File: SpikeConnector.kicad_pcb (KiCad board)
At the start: 2 copper layers, 12 x 40 mm, 4 parts

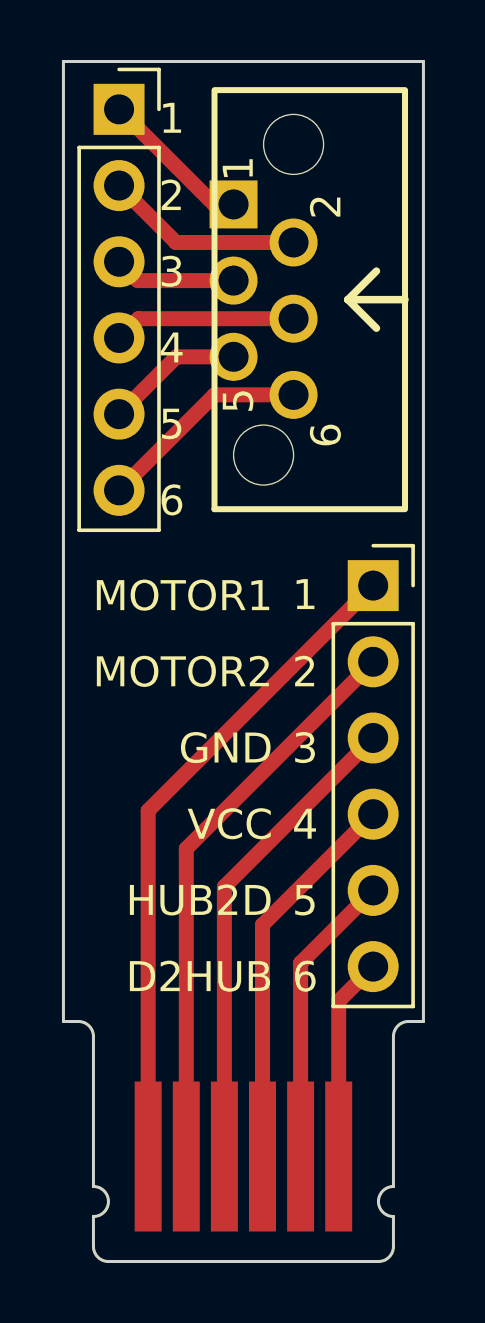
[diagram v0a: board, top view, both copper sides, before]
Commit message: Male connector fix
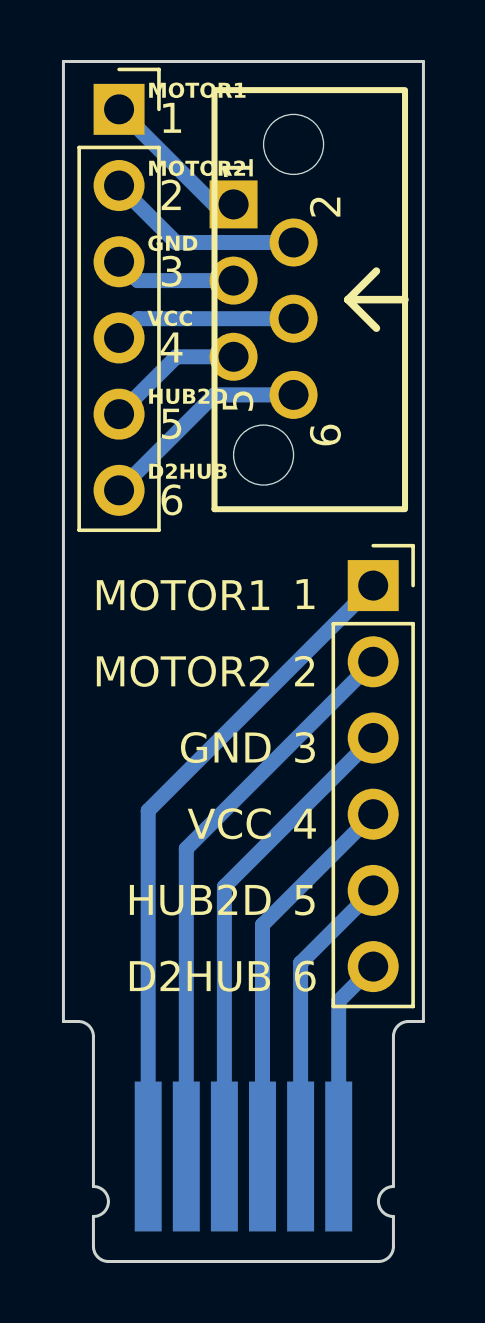
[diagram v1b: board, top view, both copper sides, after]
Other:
- board text added: "original by nicotakuya modified by drkw 25.03.27"
- board text removed: "original by nicotakuya modified by drkw 25.03.17"
